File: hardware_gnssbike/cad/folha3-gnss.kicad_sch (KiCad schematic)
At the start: 13 parts, among them J302 Hirose U.FL-R-SMT-1, U301 u-blox MAX-F10S, U302 TI TXU0204BQAR

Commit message: feat(hardware): the ERC runs, and 52 hidden errors became 4 deliberate ones
check_sch.py compared our netlist against the one KiCad extracts, pin by
pin, and was good at that and blind to everything else. KiCad's own ERC
had never been run on this schematic. It found 52 errors, and among them
a capacitor with BOTH terminals in the air.

They were of four kinds, and three of them were the drawing failing to
say what it meant rather than the circuit being wrong:

  34 open pins with no flag. The NC pins of the ESD array, the GPIOs
  nobody uses, the receiver's SDA and SCL - it speaks UART - the
  programmer's SWO. Every one of them deliberate, and indistinguishable
  from a forgotten wire. They now carry a no-connect flag, taken from
  nets.py, which is already the source of truth about what is open: a
  pin that appears in no net is open, full stop. A net with a single pin
  counts as open too, which is what R111 became when the harvester
  changed and its pull-up lost its job.

  12 rails with no source the ERC could see. The 1V8_GNSS comes from
  1V8 through a ferrite, the SD3V0_FLASH from SD3V0 through a jumper,
  the harvester's VIN from the panel. PWR_FLAG is the symbol that exists
  to say "this is supplied, I answer for it". One per ELECTRICAL GROUP,
  not per net and not per sheet: two nets that share a pin are one net
  to KiCad - the display connector carries FPC_VSS on one side and GND
  on the other through the same contact - and a flag on each side would
  be two supply outputs wired together, which is another error.

  The last one needed the electrical type to come from the symbol that
  actually reaches the sheet. The four VBUS contacts of the USB-C are
  power_out in our parts.py and passive in KiCad's symbol, so the rule
  believed the rail had a source when it had none.

What is left is four violations, and all four are the same thing: two
supply OUTPUTS wired together. KiCad calls that an error by default
because in signal circuitry two outputs on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
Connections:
- no-connect marks 0 -> 7
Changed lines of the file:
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@@
 		(stroke (width 0) (type default))
+	)
+	(no_connect
+		(at 62.230 44.450)
+	)
+	(no_connect
+		(at 52.070 31.750)
+	)
+	(no_connect
+		(at 31.750 46.990)
+	)
+	(no_connect
+		(at 31.750 49.530)
+	)
+	(no_connect
+		(at 31.750 57.150)
+	)
+	(no_connect
+		(at 78.740 46.990)
+	)
+	(no_connect
+		(at 104.140 36.830)
 	)
 	(junction
@@
 					(unit 1)
 				)
+			)
+		)
+	)
+	(symbol
+		(lib_id "power:PWR_FLAG")
+		(at 212.090 87.630 0)
+		(unit 1)
+		(exclude_from_sim no)
+		(in_bom no)
+		(on_board yes)
+		(dnp no)
+		(property "Reference" "#FLG024"
+			(at 212.09 87.63 0)
+			(effects (font (size 1.27 1.27)) (hide yes))
+		)
+		(property "Value" "PWR_FLAG"
+			(at 212.090 83.820 0)
+			(effects (font (size 1.27 1.27)))
+		)
+		(property "Footprint" ""
+			(at 212.09 87.63 0)
+			(effects (font (size 1.27 1.27)) (hide yes))
+		)
+		(property "Datasheet" ""
+			(at 212.09 87.63 0)
+			(effects (font (size 1.27 1.27)) (hide yes))
+		)
+		(pin "1")
+		(instances
+			(project "gnssbike"
+				(path "/9c874366-f223-4aef-8b18-3e2a2bab2b25/2876718e-81a5-441d-8f57-8355947cf79b"
+					(reference "#FLG024")
+					(unit 1)
+				)

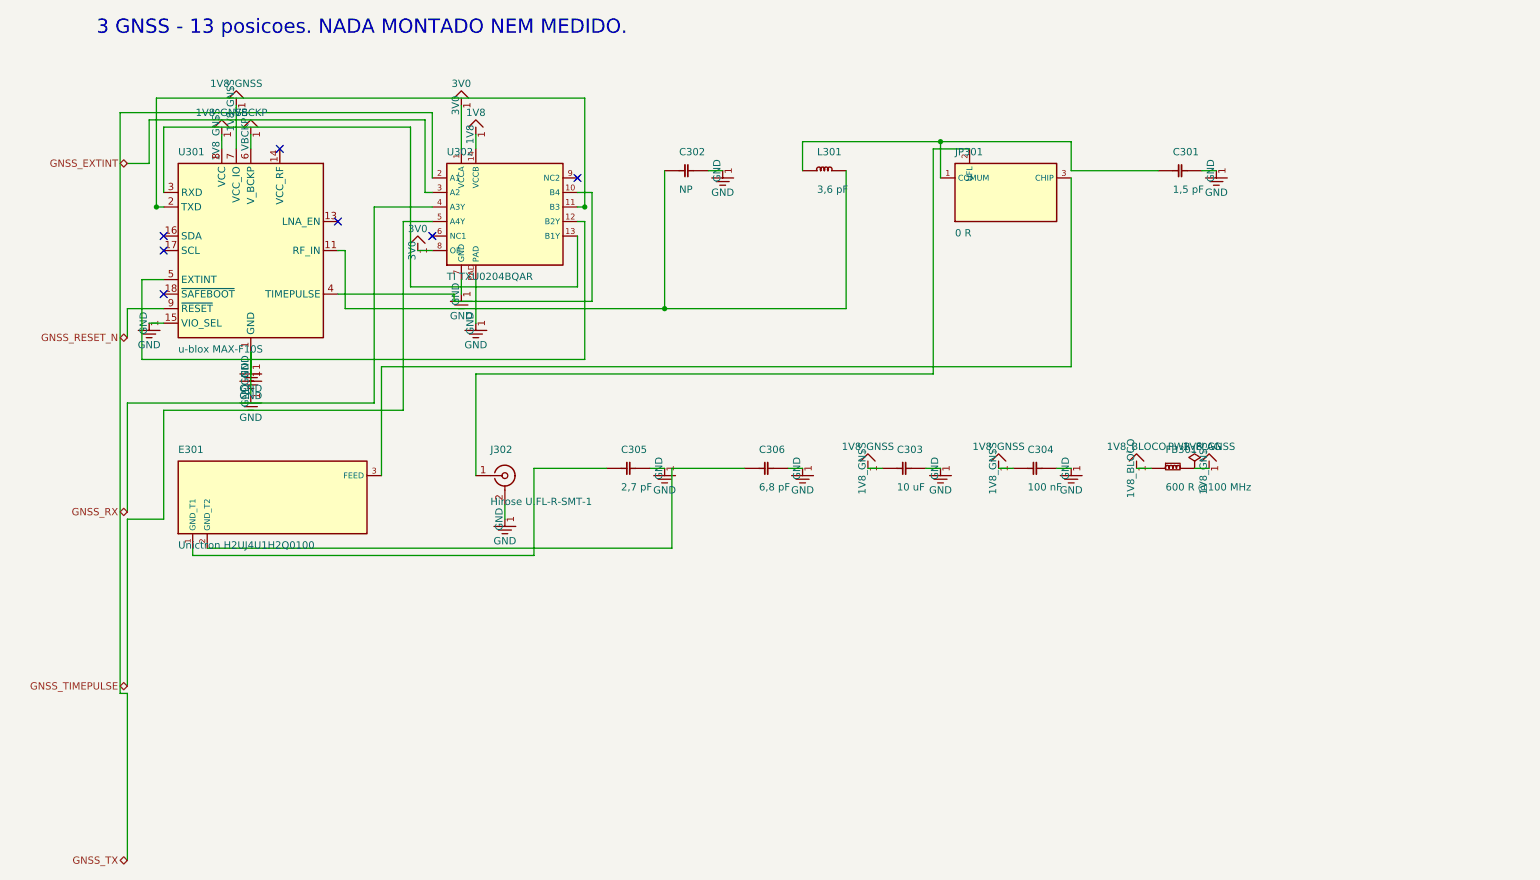
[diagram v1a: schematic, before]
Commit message: feat(hardware): GNSS receiver on the 3V0 rail, and the electrical items closed with the owner
The receiver ran at 1.8 V from BUCK1 through a TXU0204 level shifter, and
table 35 of the MAX-F10S integration manual asks +-2 % of a 1.8 V supply
where the nPM1300 buck gives +-5 %. A +-1 % LDO from 3V0 fixed the
tolerance and cost 35 mW at the battery (the receiver paid at 3.0 V with
1.2 V burnt in the LDO); option 1 of the same table - VCC and V_IO tied at
3.0 V, VIO_SEL open - costs 11 mW and removes the shifter. The owner chose
option 1. The receiver now sits on 3V0 through JP103 and the ferrite, the
four digital lines go pin to pin, the shifter and the LDO leave with four
capacitors, and BUCK1 stays fitted and unloaded as in configuration 1 of
the nPM1300 datasheet (the datasheet only shows an unused BUCK2, and what
it does not show is not copied). The devicetree follows: vcc-supply on
BUCK2, BUCK1 regulator-boot-off. The receiver no longer has a rail that
switches off; that consequence is recorded in docs/10.

Closed the same day, each a decision of the owner or a datasheet fact:

  - the ADP5091 TERM and SETSD dividers hung from BAT with REF open;
    figure 42 of the datasheet hangs all four external dividers from REF,
    which the chip switches to BAT with the hysteresis resistor in series.
    Equation 6 did not hold as drawn. Net ADP_REF, same values.
  - the solar charge thermal cut-off: the ADP5091 has no temperature
    input and the NTC divider was on the board with nobody reading it. A
    TLV7031 fed from the panel compares RT101/R106 with half of SRC and
    pulls DIS_SW high through a BAT54WS, in diode-OR with the USB divider.
    Hot side only; charging below 0 C stays open, and says so.
  - the centre key reaches P1.27 through a Schottky (D107): the SHPHLD
    node rises to 5.5 V with the cable.
  - J102 copper matched to the pinout 06 sends to the pack maker: the
    copper had VBAT+ on 1, NTC on 4, GND on 6 and 2, 3 and 5 open.
  - FB301 with 150 mO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
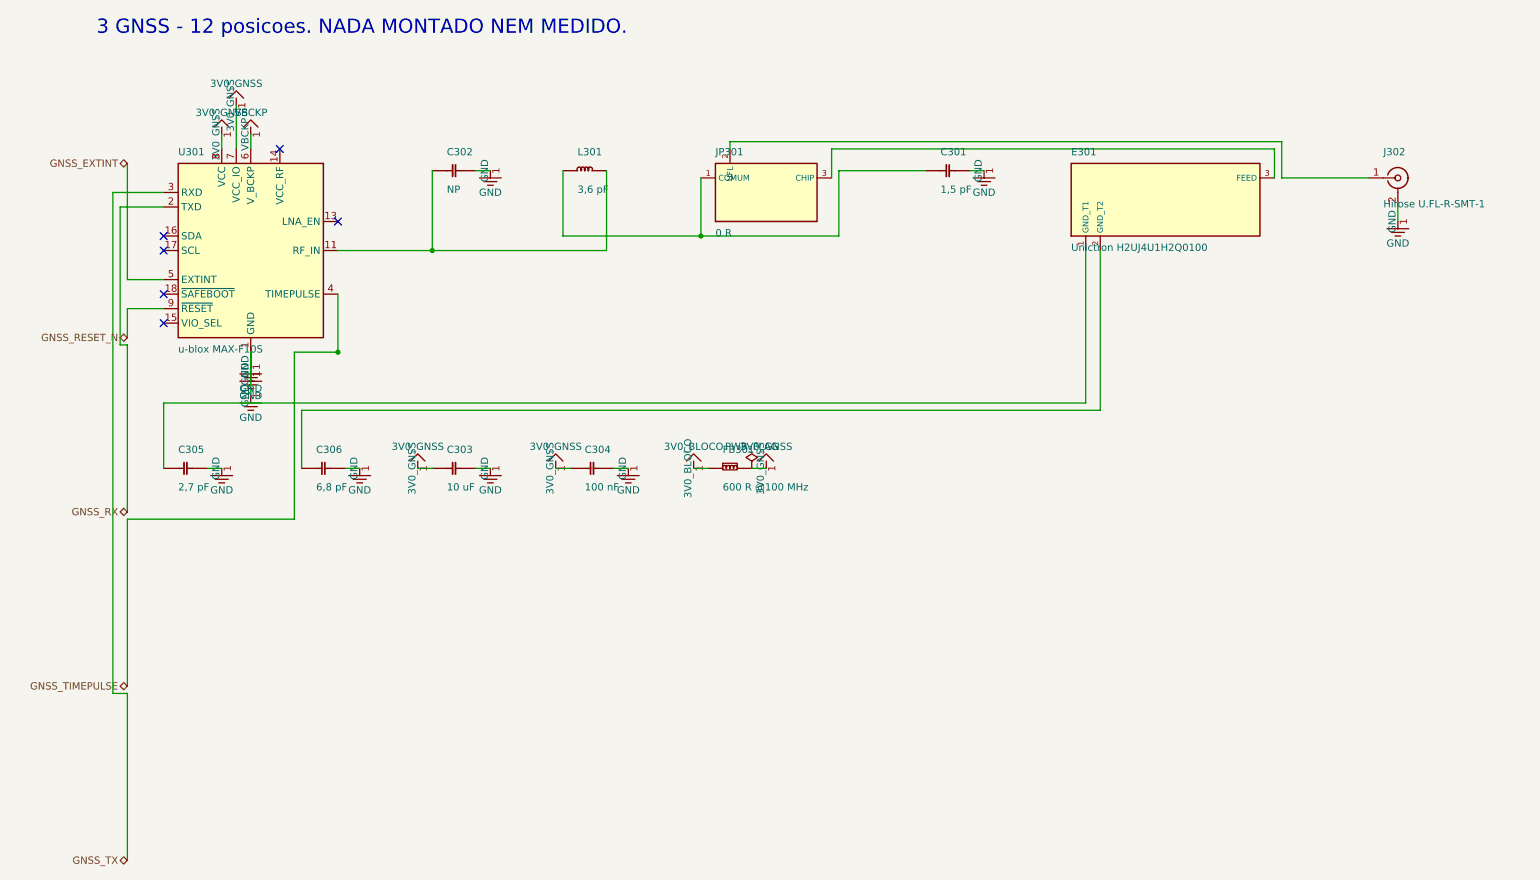
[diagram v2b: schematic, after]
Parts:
- removed U302: TI TXU0204BQAR, gnssbike:TXU0204_WQFN-14_3x2.5mm_P0.5mm, symbol gnssbike:U302
- FB301: footprint Inductor_SMD:L_0402_1005Metric -> Inductor_SMD:L_0603_1608Metric
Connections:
- net GND: no longer U301.15 (VIO_SEL)
- net GNSS_EXTINT: now also U301.5 (EXTINT)
- net GNSS_RX: now also U301.2 (TXD)
- net GNSS_TIMEPULSE: now also U301.4 (TIMEPULSE)
- net GNSS_TX: now also U301.3 (RXD)
- net 1V8_BLOCO renamed 3V0_BLOCO
- net 1V8_GNSS renamed 3V0_GNSS
- no-connect marks 7 -> 6
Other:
- note added: "3 GNSS - 12 posicoes. NADA MONTADO NEM MEDIDO."
- note removed: "3 GNSS - 13 posicoes. NADA MONTADO NEM MEDIDO."
- moved on the sheet: C301, C302, C303, C304, C305, C306, E301, FB301, J302, JP301, L301

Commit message: feat(hardware): draw the schematic by functional block, the way a person reads it
The owner asked for an industrial-standard schematic: wires and labels,
A4 or A3 pages, the right symbols and values, easy to read, the circuits
subdivided by dashed boxes. Until now each sheet was the netlist drawn as
wires - parts on a grid in connection order and a maze router pulling a
wire from every pin to wherever its other end was, across the page.

blocos.py turns each sheet into a row of functional blocks in the order
the signal flows, each in a dashed rectangle with a title: on the power
sheet, USB-C and protection, the nPM1300, the gauge and the cell, the GNSS
backup, the solar harvester, the thermal cut-off. Membership comes from
the BLOCOS table (the anchors), then make_pcb.DECOPLA and JUNTO (the
board already says whose each capacitor is), then sheets.SEGUE, then the
netlist without rails, nearest anchor by hops. Inside a block the anchor
sits in the middle and each passive beside the pin it serves, on the
side that pin faces, mirrored when the pin that serves the chip is the
far one; parts that touch only rails go to a shelf under the chip. Rails
are power symbols, neighbouring pins of one rail get a wire along their
tips and one symbol; a net that leaves its block is a local label, one
that leaves the sheet a hierarchical label, both on a short stub the
maze router bends when the straight way is taken. Sheet 1 is A3, the
rest A4, measured by the drawing itself. Decoupling capacitors now live
on their chip's sheet whatever their number.

Three KiCad 8 facts were measured with kicad-cli's netlist export on the
way, because the first version assumed each one wrong and check_sch.py
caught it: (mirror x) swaps left for right, not (mirror y); a local label
named after a rail is the net /sheet/RAIL, another net; and a pin in the
middle of a long wire is not on it - "wires connect with other wires or
pins only if their ends coincide exactly" (Eeschema manual). The
conventions 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
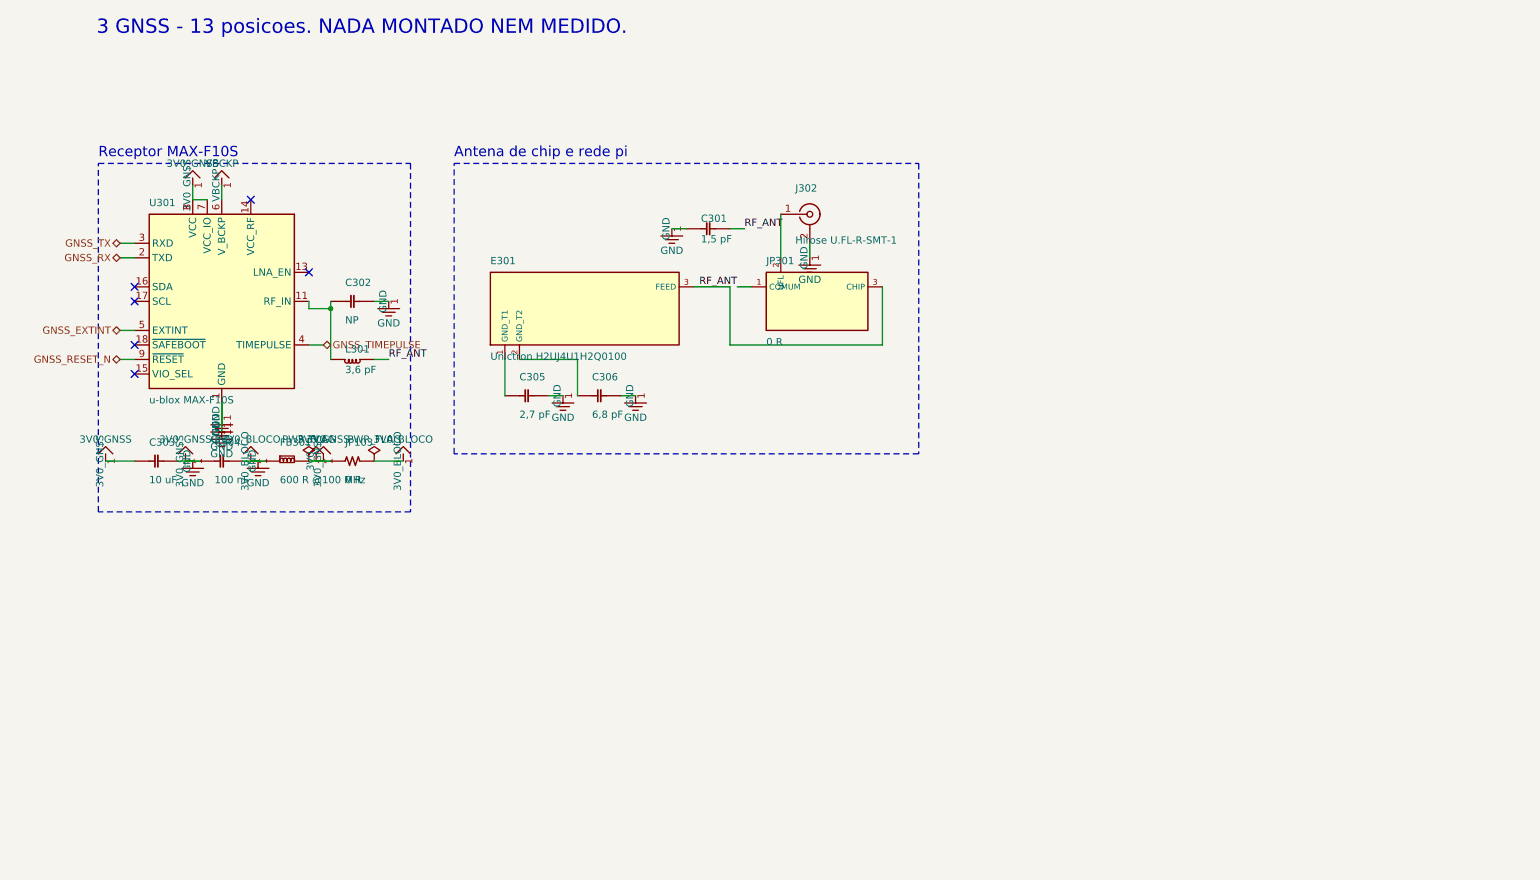
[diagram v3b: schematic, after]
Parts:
- added JP103: 0 R, Resistor_SMD:R_0402_1005Metric, symbol gnssbike:JP103
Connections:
- net 3V0_GNSS is gone; now on net 3V0: C303.1, C304.1, FB301.2, U301.7 (VCC_IO), U301.8 (VCC)
- net GND is gone; now on net 3V0: C301.2, C302.2, C303.2, C304.2, C305.2, C306.2, J302.2 (Ext), U301.1 (GND), U301.10 (GND), U301.12 (GND)
- net RF_ANT: now reaches C301.1, JP301.1 (COMUM), L301.1
- net 3V0_BLOCO renamed 3V0
- net 3V0: now also JP103.1, JP103.2
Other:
- note added: "3 GNSS - 13 posicoes. NADA MONTADO NEM MEDIDO."
- note added: "Antena de chip e rede pi"
- note added: "Receptor MAX-F10S"
- note removed: "3 GNSS - 12 posicoes. NADA MONTADO NEM MEDIDO."
- moved on the sheet: C301, C302, C303, C304, C305, C306, E301, FB301, J302, JP301, L301, U301

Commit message: feat(hardware): spread the schematic so references, values and labels stay apart
The owner asked for the block-drawn schematic to be readable: designators
and labels were printing over each other. Power symbols now hide the pin
number and name (each printed a "1" and the rail's name twice) and point
away from their pin, lying along the line of a side pin with the name on
that line; the decoupling shelf is a row of stood-up capacitors per rail
with one wire along the tops and one symbol per row, test points standing
too; references and values sit to the right of a standing part and between
the neighbouring lines of a lying one, and block titles, part texts and
symbol names are obstacles for the router and for symbol and label
placement. Pull-ups and pull-downs of a labelled line stand past the label,
and off the corridor when the line goes on to another anchor; the labels'
room is reserved before the members are placed; the FPC connector is
mirrored to face the panel and aligned with it, its board-side wire
continuing from the label point, with the two nets of a pass-through pin
allowed to share cells; the two cells in front of every pin belong to its
net; DISP_VDD is drawn as a rail; blocks are packed by height and sheet 1
fits an A3.

The library symbol now always holds the base drawing and the instance
carries the rotation and mirror. The generator used to write the library
already flipped and the (mirror ...) token as well, applying the transform
twice, and the earlier "measurement" of (mirror x) was inverted by that.
Measured again on minimal files: (mirror y) swaps left for right, an
instance at 90 sends the left pin to the bottom, and KiCad transforms the
field justification along with the instance.

check_sch.py passes: the netlist equals nets.py pin by pin, no new ERC
error, no wire over a component. Eight nets are closed by labels where the
maze found no path inside the block, and the solar harvester and the left
of the gauge remain crowded; SCH_DEBUG=1 exp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
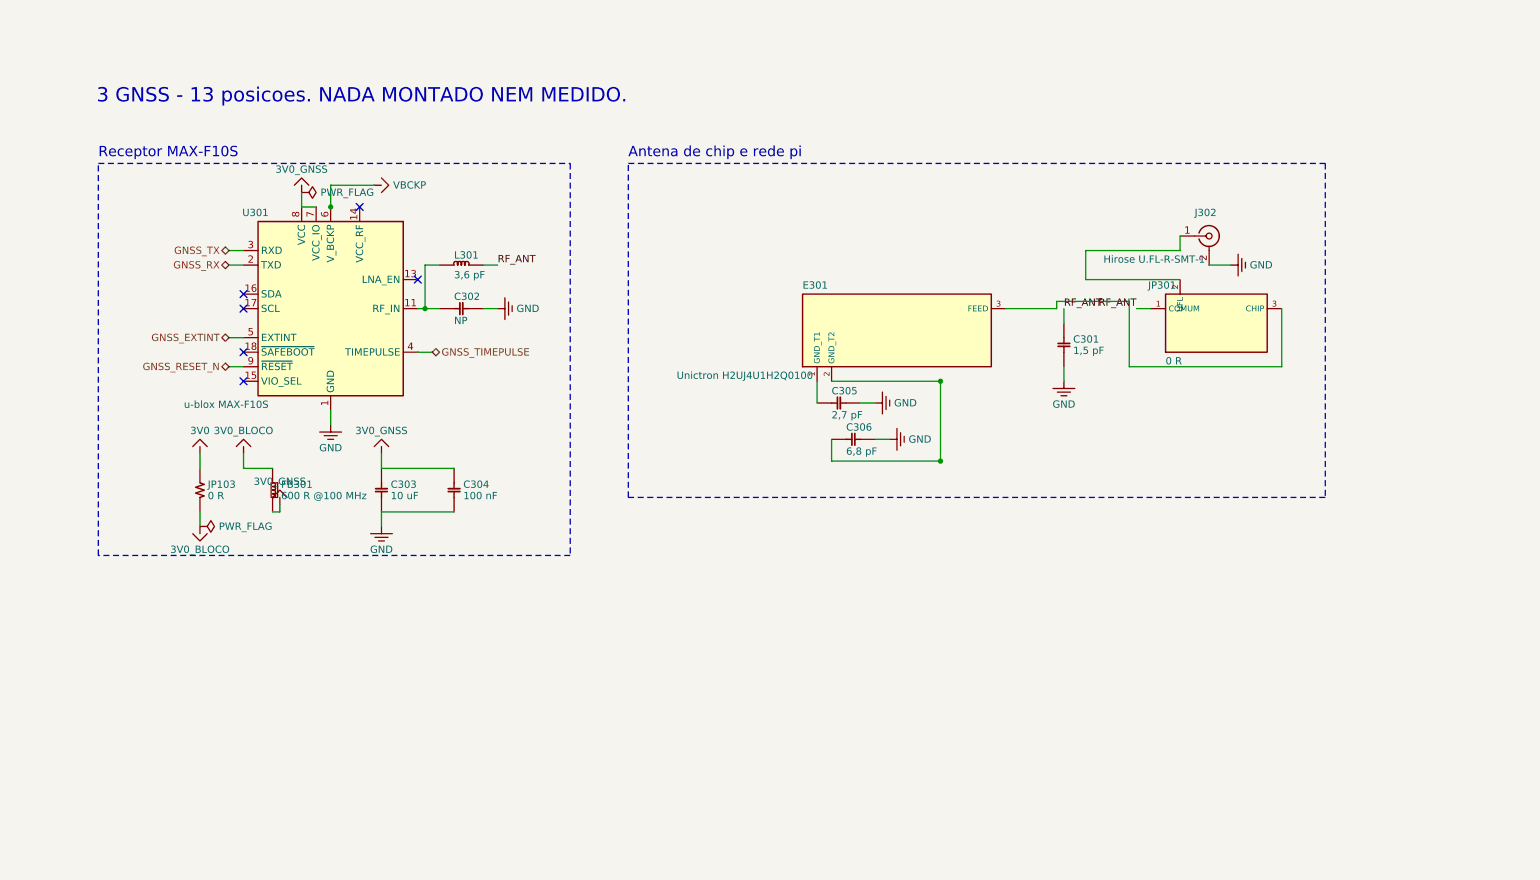
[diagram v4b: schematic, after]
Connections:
- net 3V0: no longer C301.2, C302.2, C303.1, C303.2, C304.1, C304.2, C305.2, C306.2, FB301.1, FB301.2, J302.2 (Ext), JP103.2, U301.1 (GND), U301.10 (GND), U301.12 (GND), U301.7 (VCC_IO), U301.8 (VCC)
- new net 3V0_BLOCO: FB301.1, JP103.2
- new net 3V0_GNSS: C303.1, C304.1, FB301.2, U301.7 (VCC_IO), U301.8 (VCC)
- new net GND: C301.2, C302.2, C303.2, C304.2, C305.2, C306.2, J302.2 (Ext), U301.1 (GND), U301.10 (GND), U301.12 (GND)
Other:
- moved on the sheet: C301, C302, C303, C304, C305, C306, E301, FB301, J302, JP103, JP301, L301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
